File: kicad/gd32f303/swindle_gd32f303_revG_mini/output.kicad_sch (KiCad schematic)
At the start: 2 parts, among them J1 Debug port, J2 Debug port

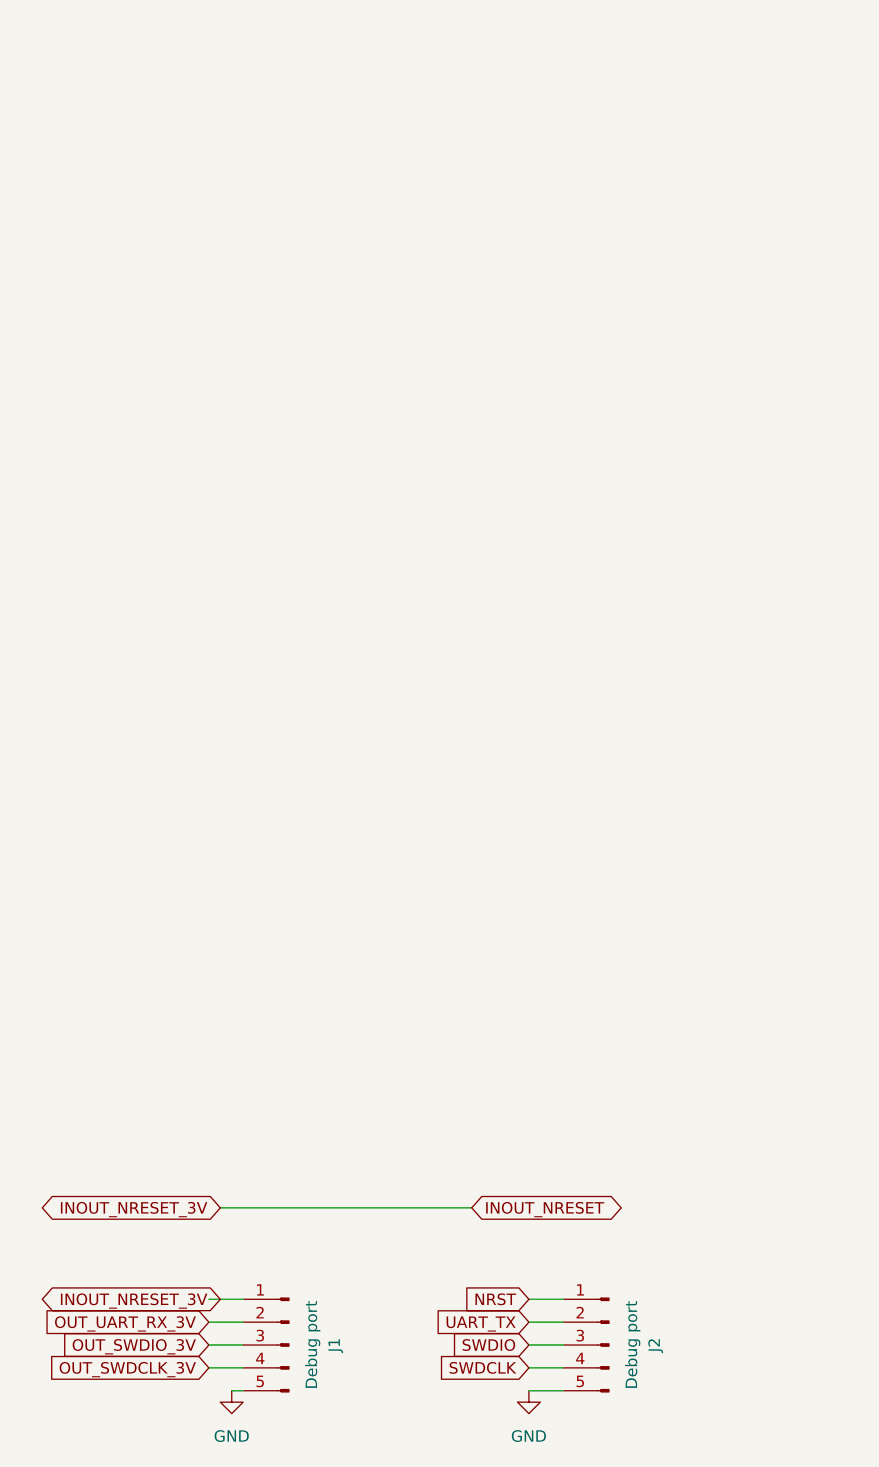
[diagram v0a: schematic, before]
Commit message: kicad: add pullup resistor on GD32/48 version
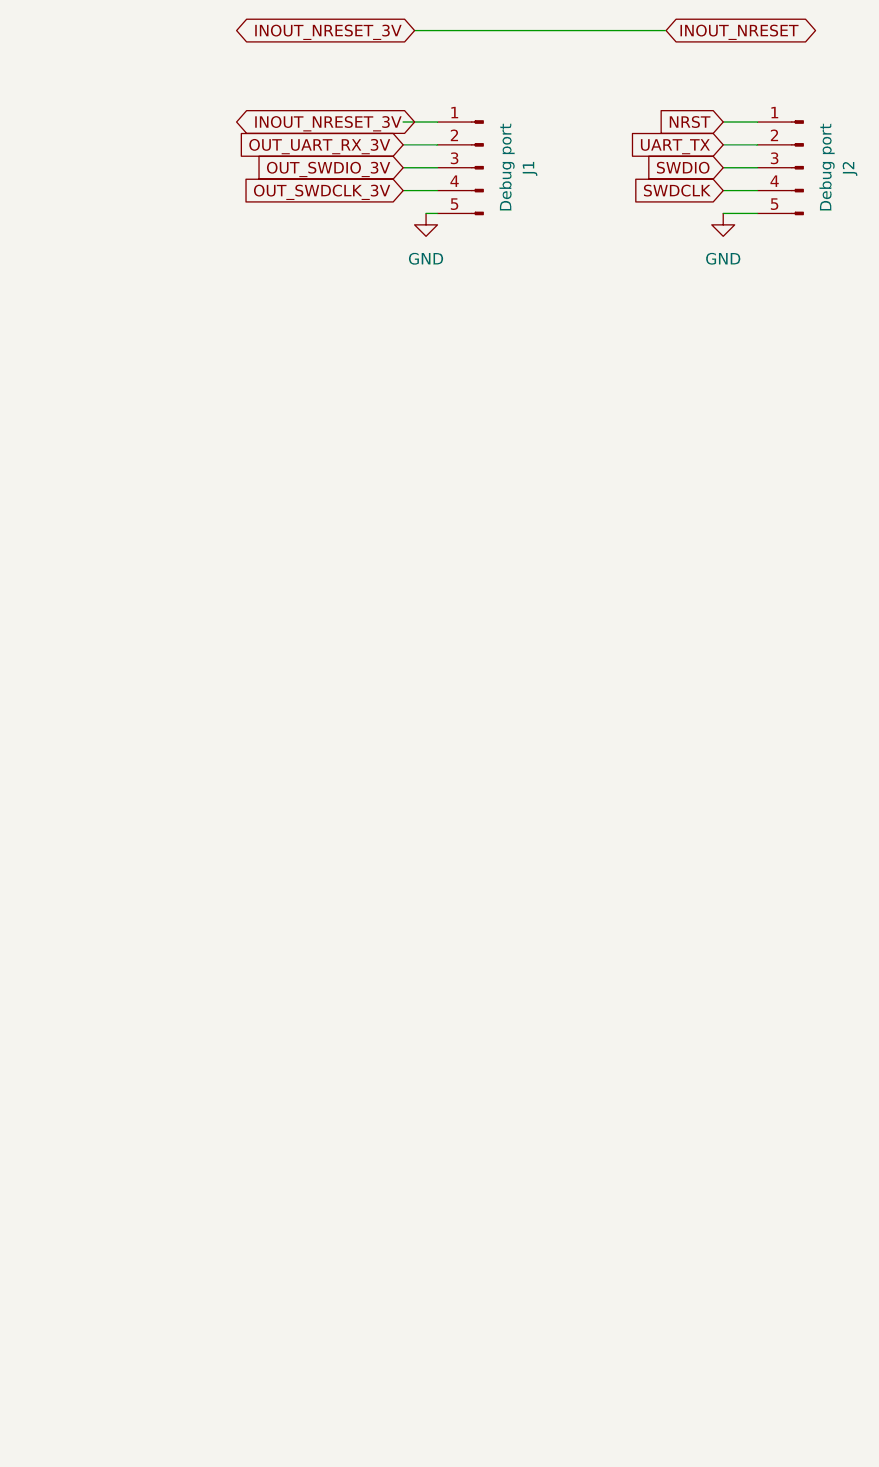
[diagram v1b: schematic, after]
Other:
- moved on the sheet: J1, J2
